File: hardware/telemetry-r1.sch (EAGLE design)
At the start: 105 parts, among them IC1 COPERNICUSSMD, IC10 TPS70933, IC2 TPS70933, IC3 74HC137, IC4 STM32L073CZT6, IC5 TPS62160, IC6 HX1, IC7 LMP7702, IC8 ADXL345, IC9 HIH9131, J1 I2C1, J10 TEMP_BAT, J11 DNP, J12 INSOL, J13 LORA, J2 I2C2, J3 BOTTOM, J4 USD-SOCKET, J5 BAT, J6 SMA_EDGE, J7 SMA_EDGE, J8 TEMP_GPS, J9 TEMP_HOT, Y1 32768, Y2 8M

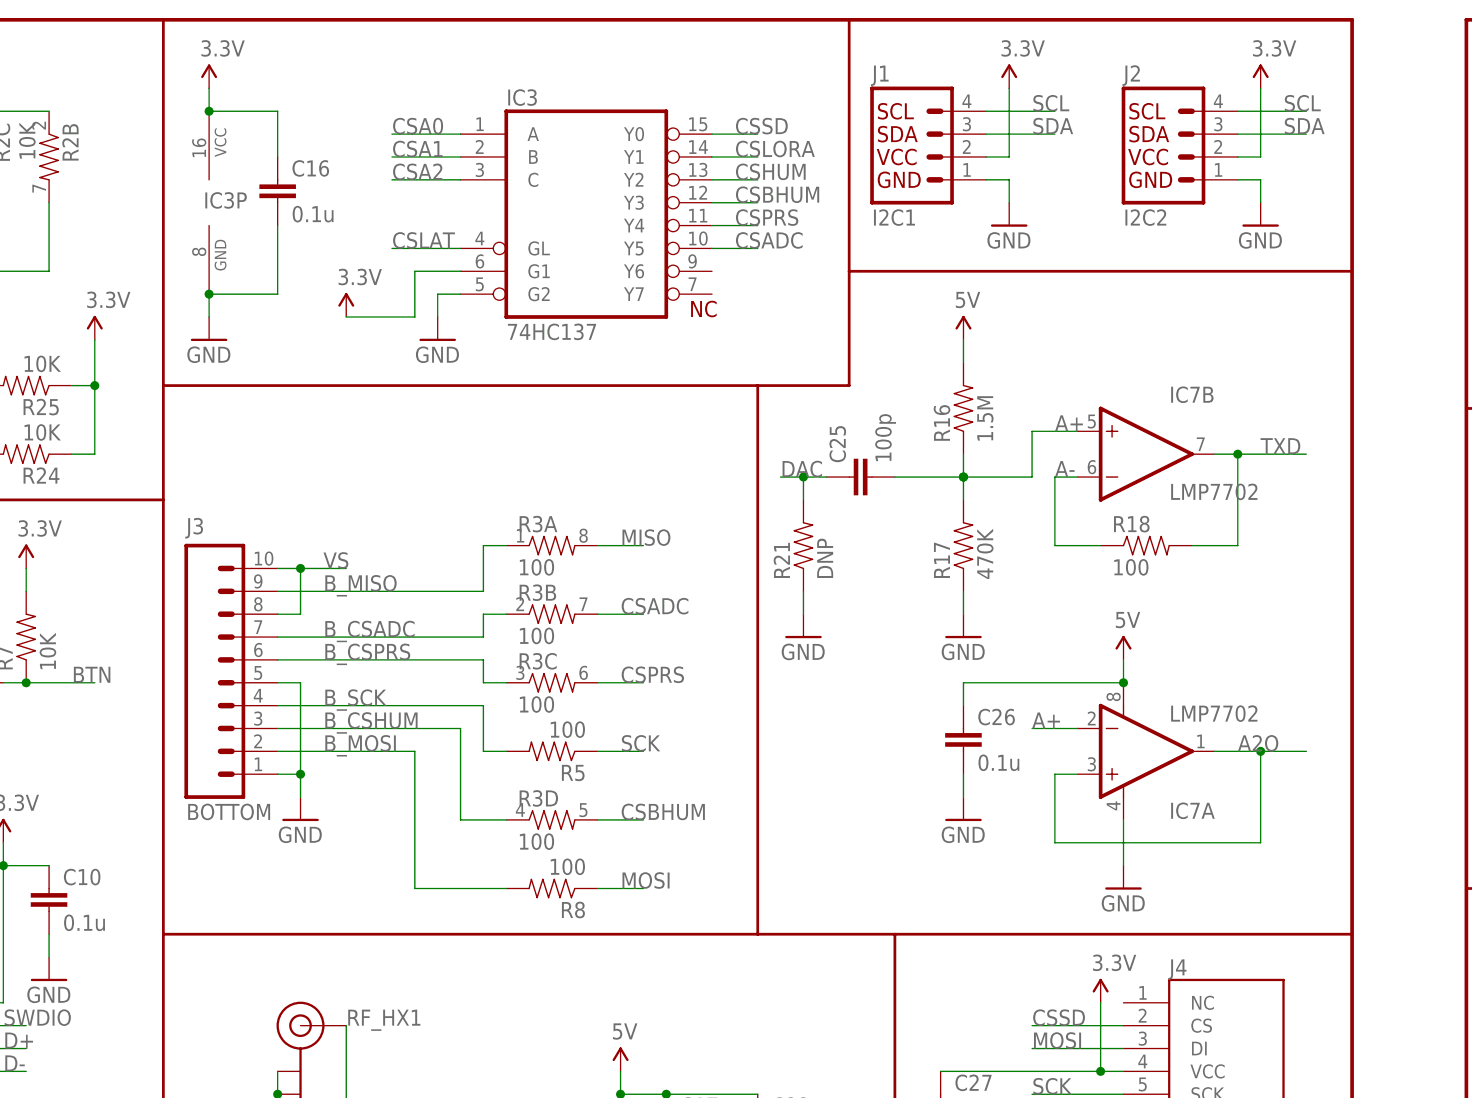
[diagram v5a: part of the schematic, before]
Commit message: Update telemetry board to include Pavel's new LPF
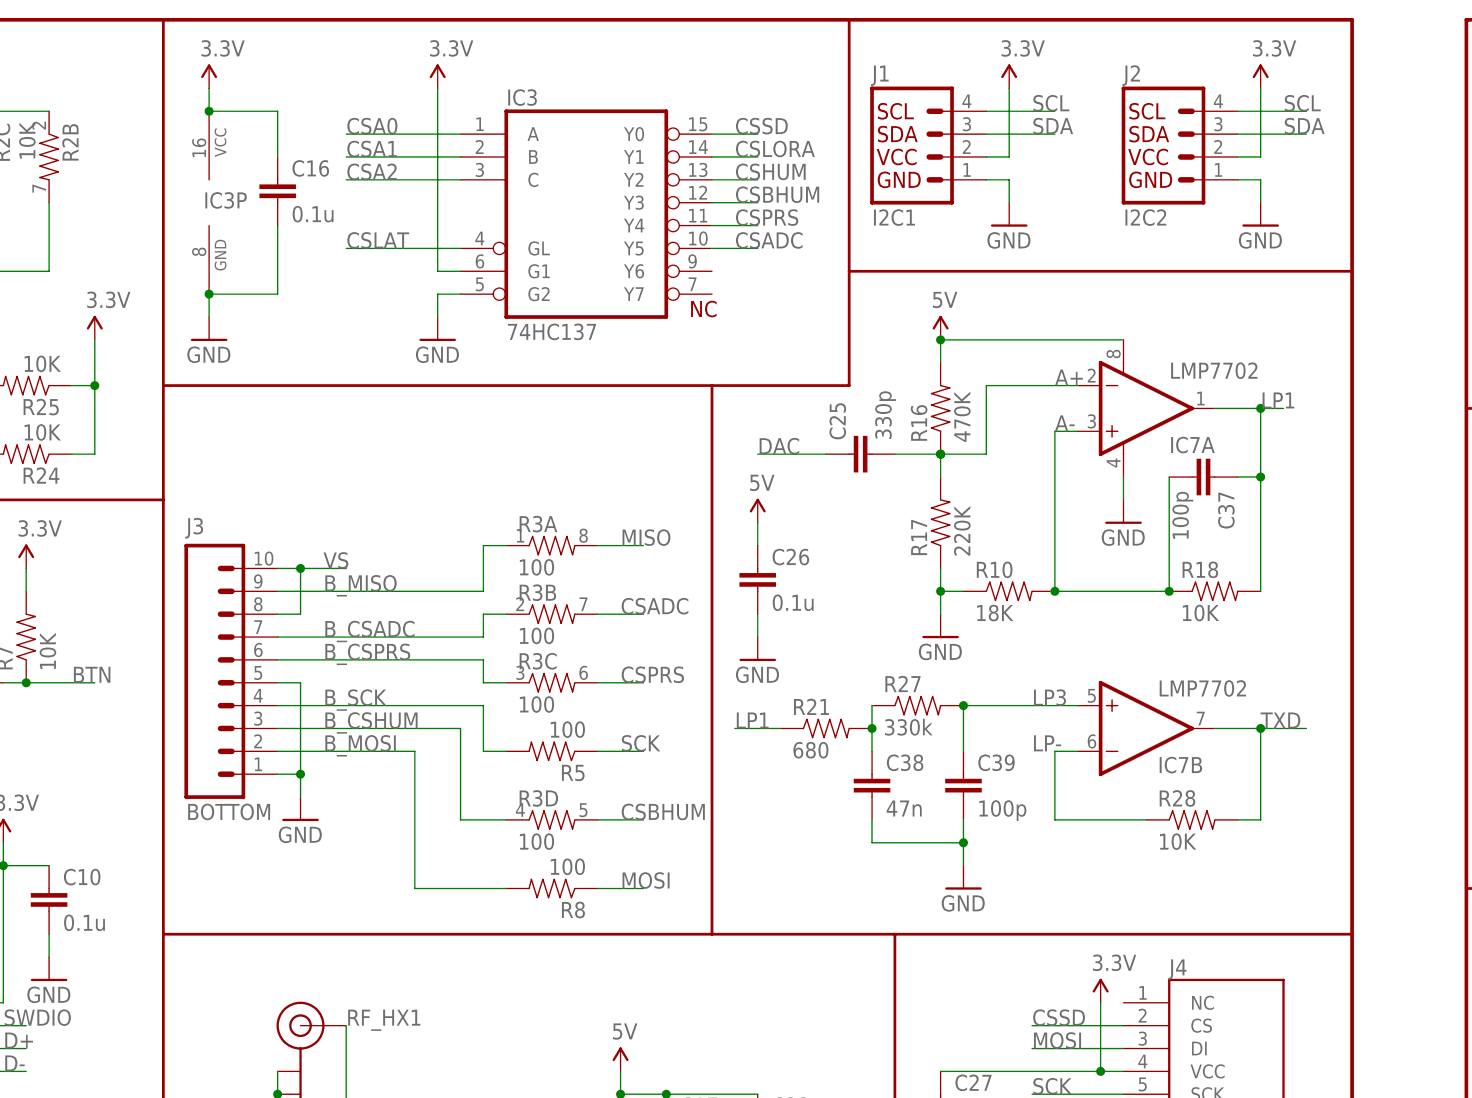
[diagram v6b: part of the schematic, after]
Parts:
- added C37, C39: 100p, SparkFun-Passives:CAP0805
- added C38: 47n, SparkFun-Passives:CAP0805
- added R10: 18K, SparkFun-Passives:RESISTOR0805-RES
- added R27: 330k, SparkFun-Passives:RESISTOR0805-RES
- added R28: 10K, SparkFun-Passives:RESISTOR0805-RES
- C25: value 100p -> 330p
- R16: value 1.5M -> 470K
- R17: value 470K -> 220K
- R18: value 100 -> 10K
- R21: value DNP -> 680
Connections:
- removed net A2O: IC7A.+IN, IC7A.OUT
- new net LP-: IC7B.-IN, R28.1
- new net LP1: C37.1, IC7A.OUT, R18.2, R21.1
- new net LP2: C38.1, R21.2, R27.1
- new net LP3: C39.1, IC7B.+IN, R27.2
- net A+: no longer IC7B.+IN
- net A-: now also C37.2, IC7A.+IN, R10.2; no longer IC7B.-IN
- net DAC: no longer R21.2
- net GND: now also C38.2, C39.2, R10.1; no longer R21.1
- net TXD: now also R28.2; no longer R18.2
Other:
- moved on the sheet: C25, C26, IC7A, IC7B, R16, R17, R18, R21

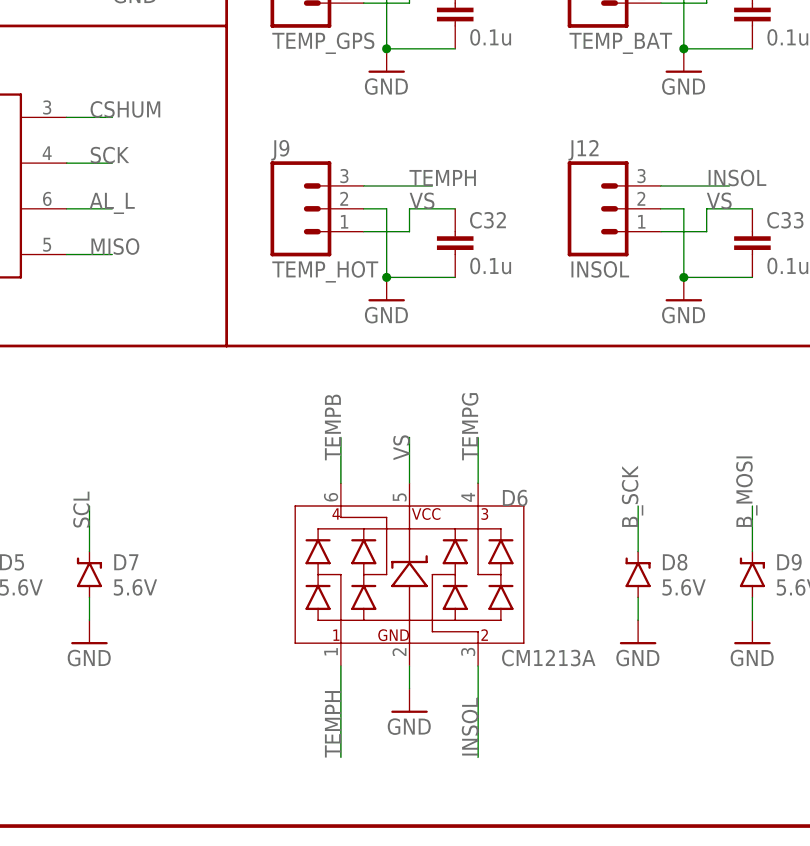
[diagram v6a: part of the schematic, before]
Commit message: Fix broken photocell routing
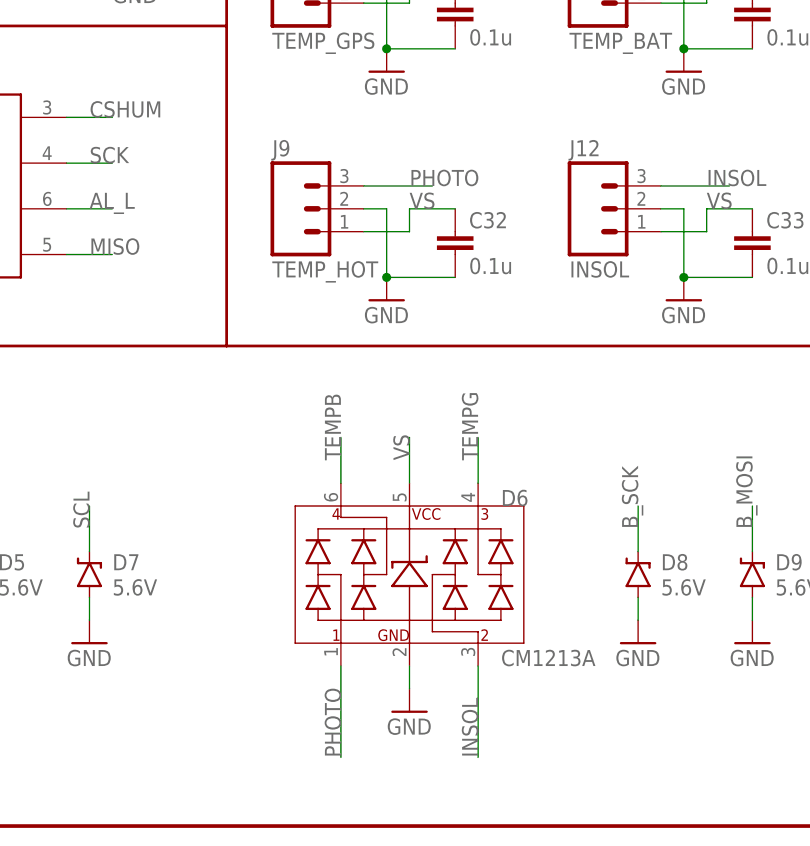
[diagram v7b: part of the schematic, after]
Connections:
- removed net TEMPH: D6.CH1, J9.3
- net PHOTO: now also D6.CH1, J9.3
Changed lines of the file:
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@@
-</segment>
-</net>
-<net name="TEMPH" class="0">
-<segment>
-<pinref part="J9" gate="J$1" pin="3"/>
-<wire x1="355.6" y1="71.12" x2="347.98" y2="71.12" width="0.1524" layer="91"/>
-<label x="353.06" y="71.12" size="1.778" layer="95"/>
-</segment>
-<segment>
-<pinref part="D6" gate="G$1" pin="CH1"/>
-<wire x1="345.44" y1="7.62" x2="345.44" y2="17.78" width="0.1524" layer="91"/>
-<label x="345.44" y="7.62" size="1.778" layer="95" rot="R90"/>
 </segment>
 </net>
@@
 <label x="35.56" y="50.8" size="1.778" layer="95"/>
 </segment>
-</net>
+<segment>
+<pinref part="J9" gate="J$1" pin="3"/>
+<wire x1="355.6" y1="71.12" x2="347.98" y2="71.12" width="0.1524" layer="91"/>
+<label x="353.06" y="71.12" size="1.778" layer="95"/>
+</segment>
+<segment>
+<pinref part="D6" gate="G$1" pin="CH1"/>
+<wire x1="345.44" y1="7.62" x2="345.44" y2="17.78" width="0.1524" layer="91"/>
+<label x="345.44" y="7.62" size="1.778" layer="95" rot="R90"/>
+</segment>
+</net>

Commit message: renamed ADC ports to use GoPro4/2 is running photo sensors
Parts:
- J12: value INSOL -> PHOTO_GP2
- J9: value TEMP_HOT -> PHOTO_GP4
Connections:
- net INSOL renamed PHOTO_GP2
- net PHOTO renamed PHOTO_GP4
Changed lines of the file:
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@@
 <?xml version="1.0" encoding="utf-8"?>
 <!DOCTYPE eagle SYSTEM "eagle.dtd">
-<eagle version="7.6.0">
+<eagle version="7.5.0">
 <drawing>
 <settings>
@@
 <part name="GND32" library="SparkFun-Aesthetics" deviceset="GND" device=""/>
 <part name="J8" library="SparkFun-Connectors" deviceset="M03" device="JST-PTH" value="TEMP_GPS"/>
-<part name="J9" library="SparkFun-Connectors" deviceset="M03" device="JST-PTH" value="TEMP_HOT"/>
+<part name="J9" library="SparkFun-Connectors" deviceset="M03" device="JST-PTH" value="PHOTO_GP4"/>
 <part name="J10" library="SparkFun-Connectors" deviceset="M03" device="JST-PTH" value="TEMP_BAT"/>
 <part name="GND33" library="SparkFun-Aesthetics" deviceset="GND" device=""/>
@@
 <part name="D6" library="HAB" deviceset="CM1213A" device="" value="CM1213A"/>
 <part name="GND38" library="SparkFun-Aesthetics" deviceset="GND" device=""/>
-<part name="J12" library="SparkFun-Connectors" deviceset="M03" device="JST-PTH" value="INSOL"/>
+<part name="J12" library="SparkFun-Connectors" deviceset="M03" device="JST-PTH" value="PHOTO_GP2"/>
 <part name="GND41" library="SparkFun-Aesthetics" deviceset="GND" device=""/>
 <part name="C33" library="SparkFun-Passives" deviceset="CAP" device="0805" value="0.1u"/>
@@
 </segment>
 </net>
-<net name="INSOL" class="0">
+<net name="PHOTO_GP2" class="0">
 <segment>
 <pinref part="J12" gate="J$1" pin="3"/>
@@
 </segment>
 </net>
-<net name="PHOTO" class="0">
+<net name="PHOTO_GP4" class="0">
 <segment>
 <pinref part="IC4" gate="G$1" pin="PA2"/>
